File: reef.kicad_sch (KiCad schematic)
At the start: 61 parts, among them J1 Conn_01x05_Female, J2 Conn_01x02_Male, U1 nice_nano, U2 TRRS, U3 TRRS

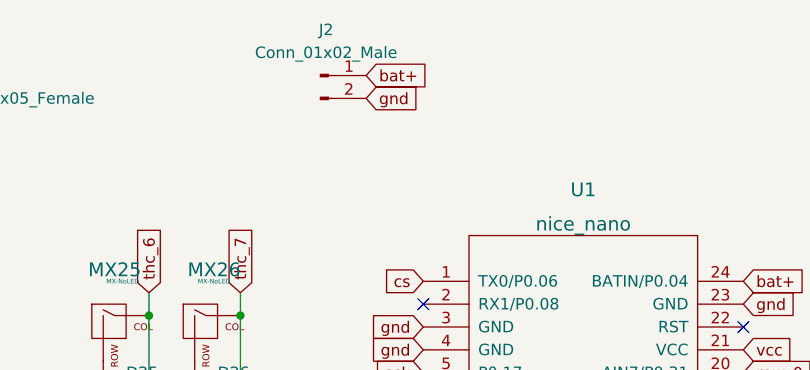
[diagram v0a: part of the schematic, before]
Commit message: Routed Battery Connector
routed traces for battery connector
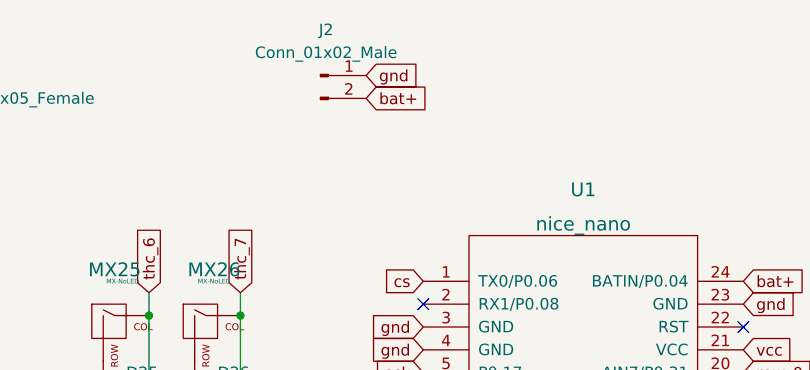
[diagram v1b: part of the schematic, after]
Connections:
- net bat+: now also J2.2 (Pin_2); no longer J2.1 (Pin_1)
- net gnd: now also J2.1 (Pin_1); no longer J2.2 (Pin_2)
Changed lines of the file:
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@@
     )
   )
-  (global_label "bat+" (shape input) (at 179.07 87.63 0) (fields_autoplaced)
+  (global_label "bat+" (shape input) (at 179.07 90.17 0) (fields_autoplaced)
     (effects (font (size 1.27 1.27)) (justify left))
-    (property "Intersheet References" "${INTERSHEET_REFS}" (id 0) (at 186.0793 87.5506 0)
+    (property "Intersheet References" "${INTERSHEET_REFS}" (id 0) (at 186.0793 90.0906 0)
       (effects (font (size 1.27 1.27)) (justify left) hide)
     )
@@
     )
   )
-  (global_label "gnd" (shape input) (at 179.07 90.17 0) (fields_autoplaced)
+  (global_label "gnd" (shape input) (at 179.07 87.63 0) (fields_autoplaced)
     (effects (font (size 1.27 1.27)) (justify left))
-    (property "Intersheet References" "${INTERSHEET_REFS}" (id 0) (at 184.9302 90.0906 0)
+    (property "Intersheet References" "${INTERSHEET_REFS}" (id 0) (at 184.9302 87.5506 0)
       (effects (font (size 1.27 1.27)) (justify left) hide)
     )

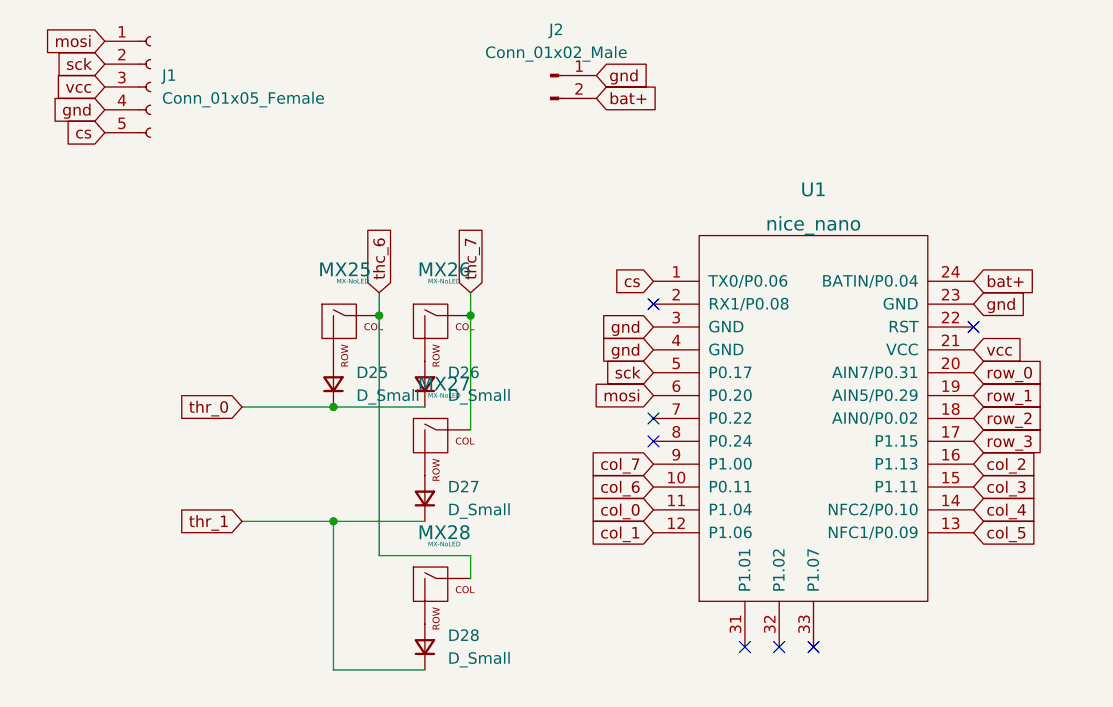
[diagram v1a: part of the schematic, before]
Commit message: Reset and Power switches in progress
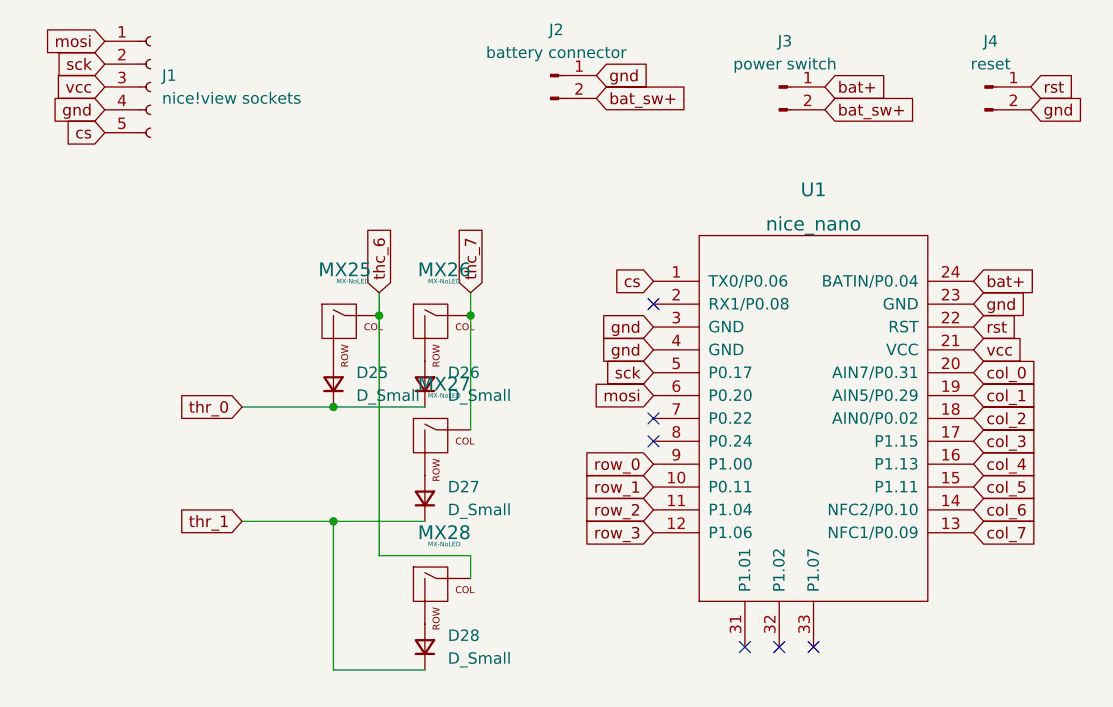
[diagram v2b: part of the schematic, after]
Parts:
- added J3: power switch, Connector_JST:JST_PH_S2B-PH-K_1x02_P2.00mm_Horizontal, symbol Connector:Conn_01x02_Male
- added J4: reset, Connector_JST:JST_PH_S2B-PH-K_1x02_P2.00mm_Horizontal, symbol Connector:Conn_01x02_Male
- J1: value Conn_01x05_Female -> nice!view sockets
- J2: value Conn_01x02_Male -> battery connector
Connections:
- net bat+: now also J3.1 (Pin_1); no longer J2.2 (Pin_2)
- net col_0: now also U1.20 (AIN7/P0.31); no longer U1.11 (P1.04)
- net col_1: now also U1.19 (AIN5/P0.29); no longer U1.12 (P1.06)
- net col_2: now also U1.18 (AIN0/P0.02); no longer U1.16 (P1.13)
- net col_3: now also U1.17 (P1.15); no longer U1.15 (P1.11)
- net col_4: now also U1.16 (P1.13); no longer U1.14 (NFC2/P0.10)
- net col_5: now also U1.15 (P1.11); no longer U1.13 (NFC1/P0.09)
- net col_6: now also U1.14 (NFC2/P0.10); no longer U1.10 (P0.11)
- net col_7: now also U1.13 (NFC1/P0.09); no longer U1.9 (P1.00)
- net gnd: now also J4.2 (Pin_2)
- net row_0: now also U1.9 (P1.00); no longer U1.20 (AIN7/P0.31)
- net row_1: now also U1.10 (P0.11); no longer U1.19 (AIN5/P0.29)
- net row_2: now also U1.11 (P1.04); no longer U1.18 (AIN0/P0.02)
- net row_3: now also U1.12 (P1.06); no longer U1.17 (P1.15)
- net rst: now reaches U1.22 (RST)
- net rst: now also J4.1 (Pin_1)
- new net bat_sw+: J2.2 (Pin_2), J3.2 (Pin_2)
- no-connect marks 7 -> 6

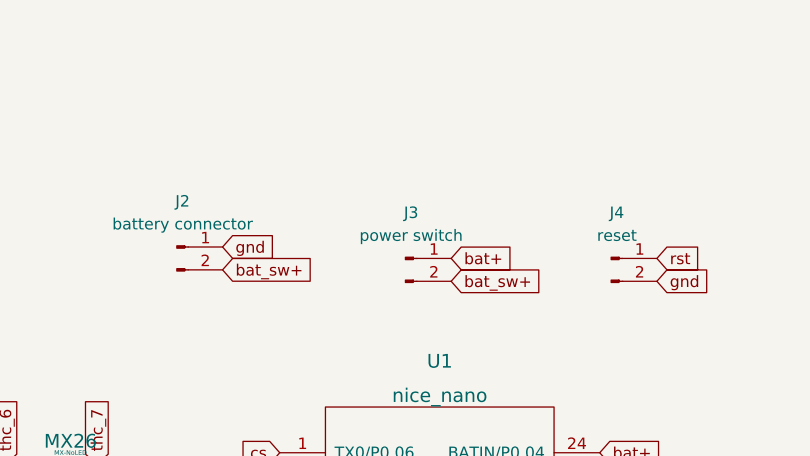
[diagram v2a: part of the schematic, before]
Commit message: Power and Reset schematics
added power and reset switches to schematic
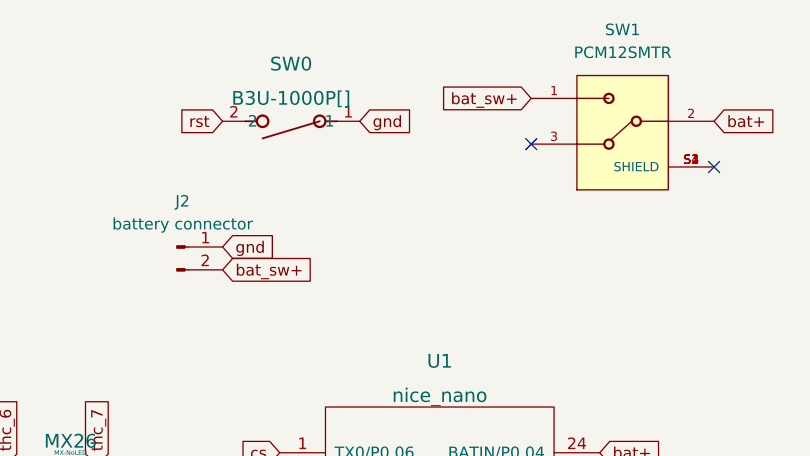
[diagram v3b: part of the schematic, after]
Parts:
- removed J3: power switch, Connector_JST:JST_PH_S2B-PH-K_1x02_P2.00mm_Horizontal, symbol Connector:Conn_01x02_Male
- removed J4: reset, Connector_JST:JST_PH_S2B-PH-K_1x02_P2.00mm_Horizontal, symbol Connector:Conn_01x02_Male
- added SW0: B3U-1000P[], SW_B3U-1000P_OMR, symbol 2023-08-22_23-55-11:B3U-1000P[]
- added SW1: PCM12SMTR, SW_PCM12SMTR, symbol PCM12SMTR:PCM12SMTR
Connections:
- net bat+: now also SW1.2
- net bat_sw+: now also SW1.1
- net gnd: now also SW0.1
- net rst: now also SW0.2
- new net: SW1.S1 (SHIELD), SW1.S2 (SHIELD), SW1.S3 (SHIELD), SW1.S4 (SHIELD)
- no-connect marks 6 -> 8
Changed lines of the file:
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@@
   (no_connect (at 203.2 151.13))
   (no_connect (at 185.42 125.73))
+  (no_connect (at 213.36 76.2))
+  (no_connect (at 233.68 78.74))
   (no_connect (at 185.42 113.03))
   (wire (pts (xy 80.01 162.56) (xy 90.17 162.56))
@@
     )
   )
+  (global_label "gnd" (shape input) (at 194.31 73.66 0) (fields_autoplaced)
+    (effects (font (size 1.27 1.27)) (justify left))
+    (property "Intersheet References" "${INTERSHEET_REFS}" (id 0) (at 200.1702 73.5806 0)
+      (effects (font (size 1.27 1.27)) (justify left) hide)
+    )
+  )
   (global_label "gnd" (shape input) (at 220.98 113.03 0) (fields_autoplaced)
     (effects (font (size 1.27 1.27)) (justify left))
@@
     )
   )
+  (global_label "bat+" (shape input) (at 233.68 73.66 0) (fields_autoplaced)
+    (effects (font (size 1.27 1.27)) (justify left))
+    (property "Intersheet References" "${INTERSHEET_REFS}" (id 0) (at 240.6893 73.5806 0)
+      (effects (font (size 1.27 1.27)) (justify left) hide)
+    )
+  )
   (global_label "col_0" (shape input) (at 220.98 120.65 0) (fields_autoplaced)
     (effects (font (size 1.27 1.27)) (justify left))
@@
     )
   )
-  (global_label "bat+" (shape input) (at 204.47 88.9 0) (fields_autoplaced)
-    (effects (font (size 1.27 1.27)) (justify left))
-    (property "Intersheet References" "${INTERSHEET_REFS}" (id 0) (at 211.4793 88.8206 0)
-      (effects (font (size 1.27 1.27)) (justify left) hide)
-    )
-  )
   (global_label "thc_6" (shape input) (at 154.94 111.76 90) (fields_autoplaced)
     (effects (font (size 1.27 1.27)) (justify left))
@@
     )
   )
-  (global_label "rst" (shape input) (at 227.33 88.9 0) (fields_autoplaced)
-    (effects (font (size 1.27 1.27)) (justify left))
-    (property "Intersheet References" "${INTERSHEET_REFS}" (id 0) (at 232.2831 88.8206 0)
-      (effects (font (size 1.27 1.27)) (justify left) hide)
-    )
-  )
   (global_label "col_7" (shape input) (at 85.09 184.15 180) (fields_autoplaced)
     (effects (font (size 1.27 1.27)) (justify right))
@@
     )
   )
-  (global_label "bat_sw+" (shape input) (at 204.47 91.44 0) (fields_autoplaced)
-    (effects (font (size 1.27 1.27)) (justify left))
-    (property "Intersheet References" "${INTERSHEET_REFS}" (id 0) (at 214.8055 91.3606 0)
-      (effects (font (size 1.27 1.27)) (justify left) hide)
-    )
-  )
   (global_label "rst" (shape input) (at 220.98 115.57 0) (fields_autoplaced)
     (effects (font (size 1.27 1.27)) (justify left))
@@
     )
   )
-  (global_label "gnd" (shape input) (at 227.33 91.44 0) (fields_autoplaced)
-    (effects (font (size 1.27 1.27)) (justify left))
-    (property "Intersheet References" "${INTERSHEET_REFS}" (id 0) (at 233.1902 91.3606 0)
-      (effects (font (size 1.27 1.27)) (justify left) hide)
+  (global_label "rst" (shape input) (at 179.07 73.66 180) (fields_autoplaced)
+    (effects (font (size 1.27 1.27)) (justify right))
+    (property "Intersheet References" "${INTERSHEET_REFS}" (id 0) (at 174.1169 73.7394 0)
+      (effects (font (size 1.27 1.27)) (justify right) hide)
     )
   )
@@
     (property "Intersheet References" "${INTERSHEET_REFS}" (id 0) (at 154.8736 173.9106 0)
       (effects (font (size 1.27 1.27)) (justify left) hide)
+    )
+  )
+  (global_label "bat_sw+" (shape input) (at 213.36 71.12 180) (fields_autoplaced)
+    (effects (font (size 1.27 1.27)) (justify right))
+    (property "Intersheet References" "${INTERSHEET_REFS}" (id 0) (at 203.0245 71.1994 0)
+      (effects (font (size 1.27 1.27)) (justify right) hide)
     )
   )
@@
     (pin "9")
   )
+  (symbol (lib_id "2023-08-22_23-55-11:B3U-1000P[]") (at 179.07 73.66 0) (unit 1)
+    (in_bom yes) (on_board yes) (fields_autoplaced)
+    (property "Reference" "SW0" (id 0) (at 186.69 67.31 0)
+      (effects (font (size 1.524 1.524)))
+    )
+    (property "Value" "B3U-1000P[]" (id 1) (at 186.69 71.12 0)
+      (effects (font (size 1.524 1.524)))
+    )
+    (property "Footprint" "SW_B3U-1000P_OMR" (id 2) (at 179.07 73.66 0)
+      (effects (font (size 1.27 1.27) italic) hide)
+    )
+    (property "Datasheet" "B3U-1000P[]" (id 3) (at 179.07 73.66 0)
+      (effects (font (size 1.27 1.27) italic) hide)
+    )
+    (pin "1")
+    (pin "2")
+  )
   (symbol (lib_id "MX_Alps_Hybrid:MX-NoLED") (at 50.8 153.67 0) (unit 1)
     (in_bom yes) (on_board yes) (fields_autoplaced)
@@
     (pin "2")
   )
-  (symbol (lib_id "Connector:Conn_01x02_Male") (at 222.25 88.9 0) (unit 1)
-    (in_bom yes) (on_board yes)
-    (property "Reference" "J4" (id 0) (at 222.885 83.82 0))
-    (property "Value" "reset" (id 1) (at 222.885 86.36 0))
-    (property "Footprint" "Connector_JST:JST_PH_S2B-PH-K_1x02_P2.00mm_Horizontal" (id 2) (at 222.25 88.9 0)
-      (effects (font (size 1.27 1.27)) hide)
-    )
-    (property "Datasheet" "~" (id 3) (at 222.25 88.9 0)
-      (effects (font (size 1.27 1.27)) hide)
-    )
-    (pin "1")
-    (pin "2")
-  )
   (symbol (lib_id "MX_Alps_Hybrid:MX-NoLED") (at 161.29 128.27 0) (unit 1)
     (in_bom yes) (on_board yes) (fields_autoplaced)
@@
     (pin "1")
     (pin "2")
+  )
+  (symbol (lib_id "PCM12SMTR:PCM12SMTR") (at 223.52 73.66 0) (unit 1)
+    (in_bom yes) (on_board yes) (fields_autoplaced)
+    (property "Reference" "SW1" (id 0) (at 223.52 63.5 0))
+    (property "Value" "PCM12SMTR" (id 1) (at 223.52 66.04 0))
+    (property "Footprint" "SW_PCM12SMTR" (id 2) (at 223.52 73.66 0)
+      (effects (font (size 1.27 1.27)) (justify bottom) hide)
+    )
+    (property "Datasheet" "" (id 3) (at 223.52 73.66 0)
+      (effects (font (size 1.27 1.27)) hide)
+    )
+    (property "DigiKey_Part_Number" "401-2016-2-ND" (id 4) (at 223.52 73.66 0)
+      (effects (font (size 1.27 1.27)) (justify bottom) hide)
+    )
+    (property "MF" "C&K" (id 5) (at 223.52 73.66 0)
+      (effects (font (size 1.27 1.27)) (justify bottom) hide)
+    )
+    (property "Purchase-URL" "https://pricing.snapeda.com/search?q=PCM12SMTR&ref=eda" (id 6) (at 223.52 73.66 0)
+      (effects (font (size 1.27 1.27)) (justify bottom) hide)
+    )
+    (property "Package" "None" (id 7) (at 223.52 73.66 0)
+      (effects (font (size 1.27 1.27)) (justify bottom) hide)
+    )
+    (property "Check_prices" "https://www.snapeda.com/parts/PCM12SMTR/C%2526K/view-part/?ref=eda" (id 8) (at 223.52 73.66 0)
+      (effects (font (size 1.27 1.27)) (justify bottom) hide)
+    )
+    (property "STANDARD" "Manufacturer Recommendation" (id 9) (at 223.52 73.66 0)
+      (effects (font (size 1.27 1.27)) (justify bottom) hide)
+    )
+    (property "SnapEDA_Link" "https://www.snapeda.com/parts/PCM12SMTR/C%2526K/view-part/?ref=snap" (id 10) (at 223.52 73.66 0)
+      (effects (font (size 1.27 1.27)) (justify bottom) hide)
+    )
+    (property "MP" "PCM12SMTR" (id 11) (at 223.52 73.66 0)
+      (effects (font (size 1.27 1.27)) (justify bottom) hide)
+    )
+    (property "Description" "\nSlide Switch SPDT Surface Mount, Right Angle\n" (id 12) (at 223.52 73.66 0)
+      (effects (font (size 1.27 1.27)) (justify bottom) hide)
+    )
+    (property "MANUFACTURER" "C&K" (id 13) (at 223.52 73.66 0)
+      (effects (font (size 1.27 1.27)) (justify bottom) hide)
+    )
+    (pin "1")
+    (pin "2")
+    (pin "3")
+    (pin "S1")
+    (pin "S2")
+    (pin "S3")
+    (pin "S4")
   )
   (symbol (lib_id "Device:D_Small") (at 69.85 121.92 90) (unit 1)
@@
     (pin "4")
   )
-  (symbol (lib_id "Connector:Conn_01x02_Male") (at 199.39 88.9 0) (unit 1)
-    (in_bom yes) (on_board yes)
-    (property "Reference" "J3" (id 0) (at 200.025 83.82 0))
-    (property "Value" "power switch" (id 1) (at 200.025 86.36 0))
-    (property "Footprint" "Connector_JST:JST_PH_S2B-PH-K_1x02_P2.00mm_Horizontal" (id 2) (at 199.39 88.9 0)
-      (effects (font (size 1.27 1.27)) hide)
-    )
-    (property "Datasheet" "~" (id 3) (at 199.39 88.9 0)
-      (effects (font (size 1.27 1.27)) hide)
-    )
-    (pin "1")
-    (pin "2")
-  )
   (symbol (lib_id "Device:D_Small") (at 149.86 121.92 90) (unit 1)
     (in_bom yes) (on_board yes) (fields_autoplaced)
@@
       (reference "J2") (unit 1) (value "battery connector") (footprint "Connector_JST:JST_PH_S2B-PH-K_1x02_P2.00mm_Horizontal")
     )
-    (path "/e61c20c1-cd07-4c16-aa80-bc82f89a9e8f"
-      (reference "J3") (unit 1) (value "power switch") (footprint "Connector_JST:JST_PH_S2B-PH-K_1x02_P2.00mm_Horizontal")
-    )
-    (path "/54048a21-d316-444b-8dcf-50936f30f7d8"
-      (reference "J4") (unit 1) (value "reset") (footprint "Connector_JST:JST_PH_S2B-PH-K_1x02_P2.00mm_Horizontal")
-    )
     (path "/78f9c3d3-3556-46f6-9744-05ad54b330f0"
       (reference "MX1") (unit 1) (value "MX-NoLED") (footprint "MX_Only:MXOnly-1U-Hotswap")
@@
       (reference "MX28") (unit 1) (value "MX-NoLED") (footprint "MX_Only:MXOnly-1.5U-Hotswap")
     )
+    (path "/1939756b-285e-4fb5-8d1e-d941f32b73ae"
+      (reference "SW0") (unit 1) (value "B3U-1000P[]") (footprint "SW_B3U-1000P_OMR")
+    )
+    (path "/5e3176f1-00ea-464b-a04b-dcb9c6b56db4"
+      (reference "SW1") (unit 1) (value "PCM12SMTR") (footprint "SW_PCM12SMTR")
+    )
     (path "/15da0337-5c17-4a0d-8eb2-6b931e23aa73"

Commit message: Traces Routed
all traces should now be fully routed
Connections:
- net col_0: now also U1.15 (P1.11); no longer U1.20 (AIN7/P0.31)
- net col_1: now also U1.16 (P1.13); no longer U1.19 (AIN5/P0.29)
- net col_2: now also U1.17 (P1.15); no longer U1.18 (AIN0/P0.02)
- net col_3: now also U1.18 (AIN0/P0.02); no longer U1.17 (P1.15)
- net col_4: now also U1.19 (AIN5/P0.29); no longer U1.16 (P1.13)
- net col_5: now also U1.20 (AIN7/P0.31); no longer U1.15 (P1.11)
- net row_0: now also U1.12 (P1.06); no longer U1.9 (P1.00)
- net row_1: now also U1.11 (P1.04); no longer U1.10 (P0.11)
- net row_2: now also U1.10 (P0.11); no longer U1.11 (P1.04)
- net row_3: now also U1.9 (P1.00); no longer U1.12 (P1.06)
